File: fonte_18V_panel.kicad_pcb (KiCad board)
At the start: 2 copper layers, 210 x 176 mm, 210 parts, among them J1 MSTBA, J2 MSTBA, J3 RJ45_Shielded, J4 RJ45_Shielded, Q1 Si2308CDS, U1 LMR16030

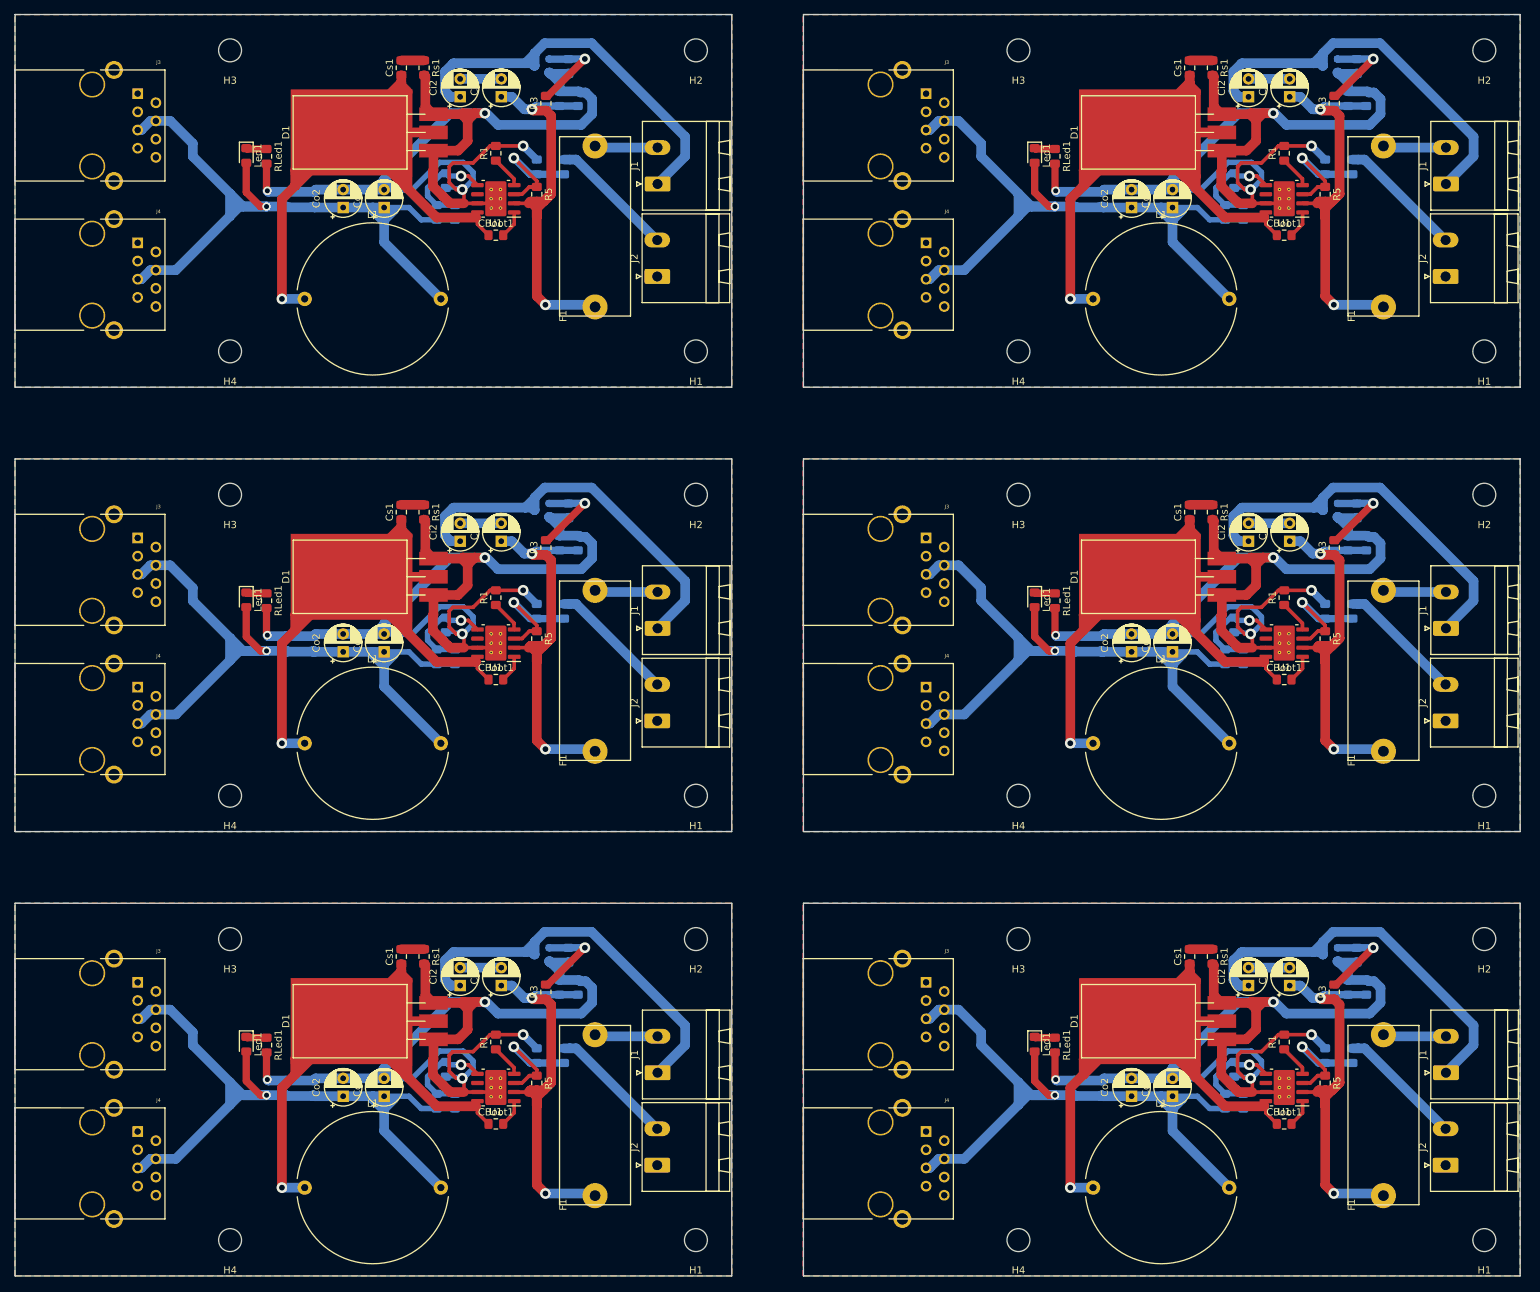
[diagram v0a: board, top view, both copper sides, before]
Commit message: Pads reforçados, algumas pequenas correções de regras
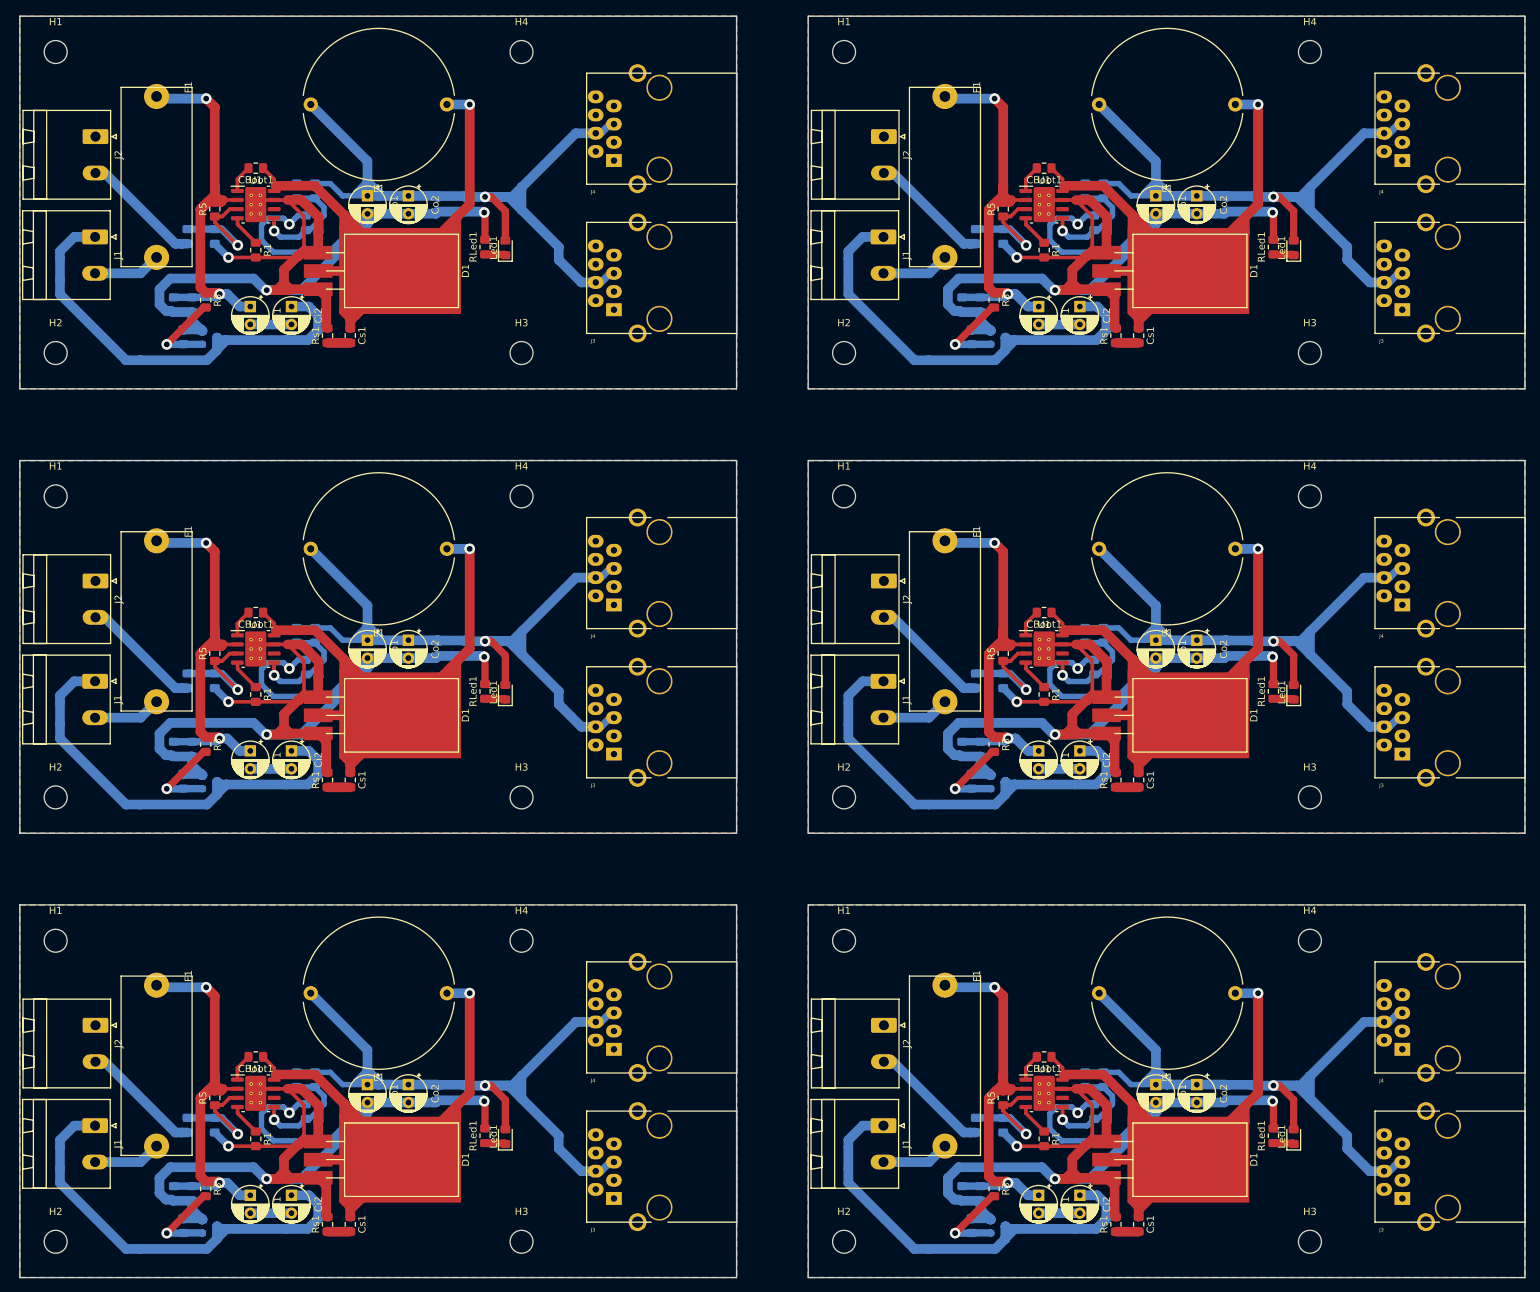
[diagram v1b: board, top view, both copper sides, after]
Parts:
- removed the CBoot1 at (221.8, 46.8)
- removed the CBoot1 at (221.8, 108.8)
- removed the CBoot1 at (221.8, 170.8)
- removed the CBoot1 at (111.8, 46.8)
- removed the CBoot1 at (111.8, 108.8)
- removed the Cff1 at (213.6, 43.6)
- removed the Cff1 at (213.6, 105.6)
- removed the Cff1 at (213.6, 167.6)
- removed the Cff1 at (103.6, 43.6)
- removed the Cff1 at (103.6, 105.6)
- removed the Ci1 at (222.6, 27.5)
- removed the Ci1 at (222.6, 89.5)
- removed the Ci1 at (222.6, 151.5)
- removed the Ci1 at (112.6, 27.5)
- removed the Ci1 at (112.6, 89.5)
- removed the Ci2 at (216.8, 27.5)
- removed the Ci2 at (216.8, 89.5)
- removed the Ci2 at (216.8, 151.5)
- removed the Ci2 at (106.8, 27.5)
- removed the Ci2 at (106.8, 89.5)
- removed the Cin2 at (230.7, 27.7)
- removed the Cin2 at (230.7, 89.7)
- removed the Cin2 at (230.7, 151.7)
- removed the Cin2 at (120.7, 27.7)
- removed the Cin2 at (120.7, 89.7)
- removed the Cin3 at (233.2, 27.7)
- removed the Cin3 at (233.2, 89.7)
- removed the Cin3 at (233.2, 151.7)
- removed the Cin3 at (123.2, 27.7)
- removed the Cin3 at (123.2, 89.7)
- removed the Co1 at (206.2, 42.9)
- removed the Co1 at (206.2, 104.9)
- removed the Co1 at (206.2, 166.9)
- removed the Co1 at (96.2, 42.9)
- removed the Co1 at (96.2, 104.9)
- removed the Co2 at (200.5, 42.9)
- removed the Co2 at (200.5, 104.9)
- removed the Co2 at (200.5, 166.9)
- removed the Co2 at (90.5, 42.9)
- removed the Co2 at (90.5, 104.9)
- removed the Co3 at (192.6, 41.7)
- removed the Co3 at (192.6, 103.7)
- removed the Co3 at (192.6, 165.7)
- removed the Co3 at (82.6, 41.7)
- removed the Co3 at (82.6, 103.7)
- removed the Co4 at (196.4, 41.7)
- removed the Co4 at (196.4, 103.7)
- removed the Co4 at (196.4, 165.7)
- removed the Co4 at (86.4, 41.7)
- removed the Co4 at (86.4, 103.7)
- removed the Cs1 at (208.6, 23.4)
- removed the Cs1 at (208.6, 85.4)
- removed the Cs1 at (208.6, 147.4)
- removed the Cs1 at (98.6, 23.4)
- removed the Cs1 at (98.6, 85.4)
- removed the D1 at (213.1, 35.0)
- removed the D1 at (213.1, 97.0)
- removed the D1 at (213.1, 159.0)
- removed the D1 at (103.1, 35.0)
- removed the D1 at (103.1, 97.0)
- removed the F1 at (230.7, 58.0)
- removed the F1 at (230.7, 120.0)
- removed the F1 at (230.7, 182.0)
- removed the F1 at (120.7, 58.0)
- removed the F1 at (120.7, 120.0)
- removed the H1 at (249.7, 63.0)
- removed the H1 at (249.7, 125.0)
- removed the H1 at (249.7, 187.0)
- removed the H1 at (139.7, 63.0)
- removed the H1 at (139.7, 125.0)
- removed the H2 at (249.7, 21.0)
- removed the H2 at (249.7, 83.0)
- removed the H2 at (249.7, 145.0)
- removed the H2 at (139.7, 21.0)
- removed the H2 at (139.7, 83.0)
- removed the H3 at (184.7, 21.0)
- removed the H3 at (184.7, 83.0)
- removed the H3 at (184.7, 145.0)
- removed the H3 at (74.7, 21.0)
- removed the H3 at (74.7, 83.0)
- removed the H4 at (184.7, 63.0)
- removed the H4 at (184.7, 125.0)
- removed the H4 at (184.7, 187.0)
- removed the H4 at (74.7, 63.0)
- removed the H4 at (74.7, 125.0)
- removed the J1 at (244.4, 39.6)
- removed the J1 at (244.4, 101.6)
- removed the J1 at (244.4, 163.6)
- removed the J1 at (134.4, 39.6)
- removed the J1 at (134.4, 101.6)
- removed the J1 at (134.4, 163.6)
- removed the J2 at (244.3, 52.5)
- removed the J2 at (244.3, 114.5)
- removed the J2 at (244.3, 176.5)
- removed the J2 at (134.3, 52.5)
- removed the J2 at (134.3, 114.5)
- removed the J2 at (134.3, 176.5)
- removed the J3 at (171.8, 27.0)
- removed the J3 at (171.8, 89.0)
- removed the J3 at (171.8, 151.0)
- removed the J3 at (61.8, 27.0)
- removed the J3 at (61.8, 89.0)
- removed the J4 at (171.8, 47.8)
- removed the J4 at (171.8, 109.8)
- removed the J4 at (171.8, 171.8)
- removed the J4 at (61.8, 47.8)
- removed the J4 at (61.8, 109.8)
- removed the L1 at (195.1, 55.6)
- removed the L1 at (195.1, 117.6)
- removed the L1 at (195.1, 179.6)
- removed the L1 at (85.1, 55.6)
- removed the L1 at (85.1, 117.6)
- removed the Led1 at (187.0, 35.6)
- removed the Led1 at (187.0, 97.6)
- removed the Led1 at (187.0, 159.6)
- removed the Led1 at (77.0, 35.6)
- removed the Led1 at (77.0, 97.6)
- removed the Q1 at (228.2, 23.1)
- removed the Q1 at (228.2, 85.1)
- removed the Q1 at (228.2, 147.1)
- removed the Q1 at (118.2, 23.1)
- removed the Q1 at (118.2, 85.1)
- removed the R1 at (221.8, 35.3)
- removed the R1 at (221.8, 97.3)
- removed the R1 at (221.8, 159.3)
- removed the R1 at (111.8, 35.3)
- removed the R1 at (111.8, 97.3)
- removed the R2 at (231.3, 37.2)
- removed the R2 at (231.3, 99.2)
- removed the R2 at (231.3, 161.2)
- removed the R2 at (121.3, 37.2)
- removed the R2 at (121.3, 99.2)
- removed the R3 at (228.8, 28.3)
- removed the R3 at (228.8, 90.3)
- removed the R3 at (228.8, 152.3)
- removed the R3 at (118.8, 28.3)
- removed the R3 at (118.8, 90.3)
- removed the R4 at (231.9, 23.2)
- removed the R4 at (231.9, 85.2)
- removed the R4 at (231.9, 147.2)
- removed the R4 at (121.9, 23.2)
- removed the R4 at (121.9, 85.2)
- removed the R5 at (227.5, 41.0)
- removed the R5 at (227.5, 103.0)
- removed the R5 at (227.5, 165.0)
- removed the R5 at (117.5, 41.0)
- removed the R5 at (117.5, 103.0)
- removed the R6 at (227.5, 37.2)
- removed the R6 at (227.5, 99.2)
- removed the R6 at (227.5, 161.2)
- removed the R6 at (117.5, 37.2)
- removed the R6 at (117.5, 99.2)
- removed the RLed1 at (189.8, 35.8)
- removed the RLed1 at (189.8, 97.8)
- removed the RLed1 at (189.8, 159.8)
- removed the RLed1 at (79.8, 35.8)
- removed the RLed1 at (79.8, 97.8)
- removed the Rfbb1 at (214.8, 39.1)
- removed the Rfbb1 at (214.8, 101.1)
- removed the Rfbb1 at (214.8, 163.1)
- removed the Rfbb1 at (104.8, 39.1)
- removed the Rfbb1 at (104.8, 101.1)
- removed the Rfbt2 at (216.1, 43.6)
- removed the Rfbt2 at (216.1, 105.6)
- removed the Rfbt2 at (216.1, 167.6)
- removed the Rfbt2 at (106.1, 43.6)
- removed the Rfbt2 at (106.1, 105.6)
- removed the Rs1 at (211.8, 23.4)
- removed the Rs1 at (211.8, 85.4)
- removed the Rs1 at (211.8, 147.4)
- removed the Rs1 at (101.8, 23.4)
- removed the Rs1 at (101.8, 85.4)
- removed the U1 at (221.8, 41.7)
- removed the U1 at (221.8, 103.7)
- removed the U1 at (221.8, 165.7)
- removed the U1 at (111.8, 41.7)
- removed the U1 at (111.8, 103.7)
- added CBoot1: 100nF, Capacitor_SMD:C_0805_2012Metric_Pad1.15x1.40mm_HandSolder, F.Cu at (188.3, 161.4)
- added CBoot1: 100nF, Capacitor_SMD:C_0805_2012Metric_Pad1.15x1.40mm_HandSolder, F.Cu at (78.3, 161.4)
- added CBoot1: 100nF, Capacitor_SMD:C_0805_2012Metric_Pad1.15x1.40mm_HandSolder, F.Cu at (188.3, 99.4)
- added CBoot1: 100nF, Capacitor_SMD:C_0805_2012Metric_Pad1.15x1.40mm_HandSolder, F.Cu at (78.3, 99.4)
- added CBoot1: 100nF, Capacitor_SMD:C_0805_2012Metric_Pad1.15x1.40mm_HandSolder, F.Cu at (188.3, 37.4)
- added Cff1: na, Capacitor_SMD:C_0805_2012Metric_Pad1.15x1.40mm_HandSolder, B.Cu at (196.6, 164.6)
- added Cff1: na, Capacitor_SMD:C_0805_2012Metric_Pad1.15x1.40mm_HandSolder, B.Cu at (86.6, 164.6)
- added Cff1: na, Capacitor_SMD:C_0805_2012Metric_Pad1.15x1.40mm_HandSolder, B.Cu at (196.6, 102.6)
- added Cff1: na, Capacitor_SMD:C_0805_2012Metric_Pad1.15x1.40mm_HandSolder, B.Cu at (86.6, 102.6)
- added Cff1: na, Capacitor_SMD:C_0805_2012Metric_Pad1.15x1.40mm_HandSolder, B.Cu at (196.6, 40.6)
- added Ci1: 10u, Capacitor_THT:CP_Radial_D5.0mm_P2.50mm, F.Cu at (187.6, 180.7)
- added Ci1: 10u, Capacitor_THT:CP_Radial_D5.0mm_P2.50mm, F.Cu at (77.6, 180.7)
- added Ci1: 10u, Capacitor_THT:CP_Radial_D5.0mm_P2.50mm, F.Cu at (187.6, 118.7)
- added Ci1: 10u, Capacitor_THT:CP_Radial_D5.0mm_P2.50mm, F.Cu at (77.6, 118.7)
- added Ci1: 10u, Capacitor_THT:CP_Radial_D5.0mm_P2.50mm, F.Cu at (187.6, 56.7)
- added Ci2: 10u, Capacitor_THT:CP_Radial_D5.0mm_P2.50mm, F.Cu at (193.3, 180.7)
- added Ci2: 10u, Capacitor_THT:CP_Radial_D5.0mm_P2.50mm, F.Cu at (83.3, 180.7)
- added Ci2: 10u, Capacitor_THT:CP_Radial_D5.0mm_P2.50mm, F.Cu at (193.3, 118.7)
- added Ci2: 10u, Capacitor_THT:CP_Radial_D5.0mm_P2.50mm, F.Cu at (83.3, 118.7)
- added Ci2: 10u, Capacitor_THT:CP_Radial_D5.0mm_P2.50mm, F.Cu at (193.3, 56.7)
- added Cin2: 100nF, Capacitor_SMD:C_0805_2012Metric_Pad1.15x1.40mm_HandSolder, B.Cu at (179.4, 180.5)
- added Cin2: 100nF, Capacitor_SMD:C_0805_2012Metric_Pad1.15x1.40mm_HandSolder, B.Cu at (69.4, 180.5)
- added Cin2: 100nF, Capacitor_SMD:C_0805_2012Metric_Pad1.15x1.40mm_HandSolder, B.Cu at (179.4, 118.5)
- added Cin2: 100nF, Capacitor_SMD:C_0805_2012Metric_Pad1.15x1.40mm_HandSolder, B.Cu at (69.4, 118.5)
- added Cin2: 100nF, Capacitor_SMD:C_0805_2012Metric_Pad1.15x1.40mm_HandSolder, B.Cu at (179.4, 56.5)
- added Cin3: 100nF, Capacitor_SMD:C_0805_2012Metric_Pad1.15x1.40mm_HandSolder, B.Cu at (176.9, 180.5)
- added Cin3: 100nF, Capacitor_SMD:C_0805_2012Metric_Pad1.15x1.40mm_HandSolder, B.Cu at (66.9, 180.5)
- added Cin3: 100nF, Capacitor_SMD:C_0805_2012Metric_Pad1.15x1.40mm_HandSolder, B.Cu at (176.9, 118.5)
- added Cin3: 100nF, Capacitor_SMD:C_0805_2012Metric_Pad1.15x1.40mm_HandSolder, B.Cu at (66.9, 118.5)
- added Cin3: 100nF, Capacitor_SMD:C_0805_2012Metric_Pad1.15x1.40mm_HandSolder, B.Cu at (176.9, 56.5)
- added Co1: 47u, Capacitor_THT:CP_Radial_D5.0mm_P2.50mm, F.Cu at (203.9, 165.3)
- added Co1: 47u, Capacitor_THT:CP_Radial_D5.0mm_P2.50mm, F.Cu at (93.9, 165.3)
- added Co1: 47u, Capacitor_THT:CP_Radial_D5.0mm_P2.50mm, F.Cu at (203.9, 103.3)
- added Co1: 47u, Capacitor_THT:CP_Radial_D5.0mm_P2.50mm, F.Cu at (93.9, 103.3)
- added Co1: 47u, Capacitor_THT:CP_Radial_D5.0mm_P2.50mm, F.Cu at (203.9, 41.3)
- added Co2: 47u, Capacitor_THT:CP_Radial_D5.0mm_P2.50mm, F.Cu at (209.6, 165.3)
- added Co2: 47u, Capacitor_THT:CP_Radial_D5.0mm_P2.50mm, F.Cu at (99.6, 165.3)
- added Co2: 47u, Capacitor_THT:CP_Radial_D5.0mm_P2.50mm, F.Cu at (209.6, 103.3)
- added Co2: 47u, Capacitor_THT:CP_Radial_D5.0mm_P2.50mm, F.Cu at (99.6, 103.3)
- added Co2: 47u, Capacitor_THT:CP_Radial_D5.0mm_P2.50mm, F.Cu at (209.6, 41.3)
- added Co3: o.1u, Capacitor_SMD:C_0805_2012Metric_Pad1.15x1.40mm_HandSolder, B.Cu at (217.6, 166.4)
- added Co3: o.1u, Capacitor_SMD:C_0805_2012Metric_Pad1.15x1.40mm_HandSolder, B.Cu at (107.6, 166.4)
- added Co3: o.1u, Capacitor_SMD:C_0805_2012Metric_Pad1.15x1.40mm_HandSolder, B.Cu at (217.6, 104.4)
- added Co3: o.1u, Capacitor_SMD:C_0805_2012Metric_Pad1.15x1.40mm_HandSolder, B.Cu at (107.6, 104.4)
- added Co3: o.1u, Capacitor_SMD:C_0805_2012Metric_Pad1.15x1.40mm_HandSolder, B.Cu at (217.6, 42.4)
- added Co4: 0.1u, Capacitor_SMD:C_0805_2012Metric_Pad1.15x1.40mm_HandSolder, B.Cu at (213.8, 166.4)
- added Co4: 0.1u, Capacitor_SMD:C_0805_2012Metric_Pad1.15x1.40mm_HandSolder, B.Cu at (103.8, 166.4)
- added Co4: 0.1u, Capacitor_SMD:C_0805_2012Metric_Pad1.15x1.40mm_HandSolder, B.Cu at (213.8, 104.4)
- added Co4: 0.1u, Capacitor_SMD:C_0805_2012Metric_Pad1.15x1.40mm_HandSolder, B.Cu at (103.8, 104.4)
- added Co4: 0.1u, Capacitor_SMD:C_0805_2012Metric_Pad1.15x1.40mm_HandSolder, B.Cu at (213.8, 42.4)
- added Cs1: 100n, Capacitor_SMD:C_0805_2012Metric_Pad1.15x1.40mm_HandSolder, F.Cu at (201.5, 184.8)
- added Cs1: 100n, Capacitor_SMD:C_0805_2012Metric_Pad1.15x1.40mm_HandSolder, F.Cu at (91.5, 184.8)
- added Cs1: 100n, Capacitor_SMD:C_0805_2012Metric_Pad1.15x1.40mm_HandSolder, F.Cu at (201.5, 122.8)
- added Cs1: 100n, Capacitor_SMD:C_0805_2012Metric_Pad1.15x1.40mm_HandSolder, F.Cu at (91.5, 122.8)
- added Cs1: 100n, Capacitor_SMD:C_0805_2012Metric_Pad1.15x1.40mm_HandSolder, F.Cu at (201.5, 60.8)
- added D1: MBR20200CTG, Package_TO_SOT_THT:TO-220-3_Horizontal_TabDown_SMD, F.Cu at (197.0, 173.2)
- added D1: MBR20200CTG, Package_TO_SOT_THT:TO-220-3_Horizontal_TabDown_SMD, F.Cu at (87.0, 173.2)
- added D1: MBR20200CTG, Package_TO_SOT_THT:TO-220-3_Horizontal_TabDown_SMD, F.Cu at (197.0, 111.2)
- added D1: MBR20200CTG, Package_TO_SOT_THT:TO-220-3_Horizontal_TabDown_SMD, F.Cu at (87.0, 111.2)
- added D1: MBR20200CTG, Package_TO_SOT_THT:TO-220-3_Horizontal_TabDown_SMD, F.Cu at (197.0, 49.2)
- added F1: 2A, KicadZeniteSolarLibrary18:Fuse_Holder_5x20, F.Cu at (179.4, 150.1)
- added F1: 2A, KicadZeniteSolarLibrary18:Fuse_Holder_5x20, F.Cu at (69.4, 150.1)
- added F1: 2A, KicadZeniteSolarLibrary18:Fuse_Holder_5x20, F.Cu at (179.4, 88.1)
- added F1: 2A, KicadZeniteSolarLibrary18:Fuse_Holder_5x20, F.Cu at (69.4, 88.1)
- added F1: 2A, KicadZeniteSolarLibrary18:Fuse_Holder_5x20, F.Cu at (179.4, 26.1)
- added H1: MountingHole, MountingHole:MountingHole_3.2mm_M3, F.Cu at (160.4, 145.2)
- added H1: MountingHole, MountingHole:MountingHole_3.2mm_M3, F.Cu at (50.4, 145.2)
- added H1: MountingHole, MountingHole:MountingHole_3.2mm_M3, F.Cu at (160.4, 83.2)
- added H1: MountingHole, MountingHole:MountingHole_3.2mm_M3, F.Cu at (50.4, 83.2)
- added H1: MountingHole, MountingHole:MountingHole_3.2mm_M3, F.Cu at (160.4, 21.2)
- added H2: MountingHole, MountingHole:MountingHole_3.2mm_M3, F.Cu at (160.4, 187.2)
- added H2: MountingHole, MountingHole:MountingHole_3.2mm_M3, F.Cu at (50.4, 187.2)
- added H2: MountingHole, MountingHole:MountingHole_3.2mm_M3, F.Cu at (160.4, 125.2)
- added H2: MountingHole, MountingHole:MountingHole_3.2mm_M3, F.Cu at (50.4, 125.2)
- added H2: MountingHole, MountingHole:MountingHole_3.2mm_M3, F.Cu at (160.4, 63.2)
- added H3: MountingHole, MountingHole:MountingHole_3.2mm_M3, F.Cu at (225.4, 187.2)
- added H3: MountingHole, MountingHole:MountingHole_3.2mm_M3, F.Cu at (115.4, 187.2)
- added H3: MountingHole, MountingHole:MountingHole_3.2mm_M3, F.Cu at (225.4, 125.2)
- added H3: MountingHole, MountingHole:MountingHole_3.2mm_M3, F.Cu at (115.4, 125.2)
- added H3: MountingHole, MountingHole:MountingHole_3.2mm_M3, F.Cu at (225.4, 63.2)
- added H4: MountingHole, MountingHole:MountingHole_3.2mm_M3, F.Cu at (225.4, 145.2)
- added H4: MountingHole, MountingHole:MountingHole_3.2mm_M3, F.Cu at (115.4, 145.2)
- added H4: MountingHole, MountingHole:MountingHole_3.2mm_M3, F.Cu at (225.4, 83.2)
- added H4: MountingHole, MountingHole:MountingHole_3.2mm_M3, F.Cu at (115.4, 83.2)
- added H4: MountingHole, MountingHole:MountingHole_3.2mm_M3, F.Cu at (225.4, 21.2)
- added J1: MSTBA, Connector_Phoenix_MSTB:PhoenixContact_MSTBA_2,5_2-G-5,08_1x02_P5.08mm_Horizontal, F.Cu at (165.9, 171.0)
- added J1: MSTBA, Connector_Phoenix_MSTB:PhoenixContact_MSTBA_2,5_2-G-5,08_1x02_P5.08mm_Horizontal, F.Cu at (55.9, 171.0)
- added J1: MSTBA, Connector_Phoenix_MSTB:PhoenixContact_MSTBA_2,5_2-G-5,08_1x02_P5.08mm_Horizontal, F.Cu at (165.9, 109.0)
- added J1: MSTBA, Connector_Phoenix_MSTB:PhoenixContact_MSTBA_2,5_2-G-5,08_1x02_P5.08mm_Horizontal, F.Cu at (55.9, 109.0)
- added J1: MSTBA, Connector_Phoenix_MSTB:PhoenixContact_MSTBA_2,5_2-G-5,08_1x02_P5.08mm_Horizontal, F.Cu at (165.9, 47.0)
- added J1: MSTBA, Connector_Phoenix_MSTB:PhoenixContact_MSTBA_2,5_2-G-5,08_1x02_P5.08mm_Horizontal, F.Cu at (55.9, 47.0)
- added J2: MSTBA, Connector_Phoenix_MSTB:PhoenixContact_MSTBA_2,5_2-G-5,08_1x02_P5.08mm_Horizontal, F.Cu at (166.0, 157.0)
- added J2: MSTBA, Connector_Phoenix_MSTB:PhoenixContact_MSTBA_2,5_2-G-5,08_1x02_P5.08mm_Horizontal, F.Cu at (56.0, 157.0)
- added J2: MSTBA, Connector_Phoenix_MSTB:PhoenixContact_MSTBA_2,5_2-G-5,08_1x02_P5.08mm_Horizontal, F.Cu at (166.0, 95.0)
- added J2: MSTBA, Connector_Phoenix_MSTB:PhoenixContact_MSTBA_2,5_2-G-5,08_1x02_P5.08mm_Horizontal, F.Cu at (56.0, 95.0)
- added J2: MSTBA, Connector_Phoenix_MSTB:PhoenixContact_MSTBA_2,5_2-G-5,08_1x02_P5.08mm_Horizontal, F.Cu at (166.0, 33.0)
- added J2: MSTBA, Connector_Phoenix_MSTB:PhoenixContact_MSTBA_2,5_2-G-5,08_1x02_P5.08mm_Horizontal, F.Cu at (56.0, 33.0)
- added J3: RJ45_Shielded, MFP19RJ45:RJ45_YH59_01, F.Cu at (238.3, 181.2)
- added J3: RJ45_Shielded, MFP19RJ45:RJ45_YH59_01, F.Cu at (128.3, 181.2)
- added J3: RJ45_Shielded, MFP19RJ45:RJ45_YH59_01, F.Cu at (238.3, 119.2)
- added J3: RJ45_Shielded, MFP19RJ45:RJ45_YH59_01, F.Cu at (128.3, 119.2)
- added J3: RJ45_Shielded, MFP19RJ45:RJ45_YH59_01, F.Cu at (238.3, 57.2)
- added J4: RJ45_Shielded, MFP19RJ45:RJ45_YH59_01, F.Cu at (238.3, 160.3)
- added J4: RJ45_Shielded, MFP19RJ45:RJ45_YH59_01, F.Cu at (128.3, 160.3)
- added J4: RJ45_Shielded, MFP19RJ45:RJ45_YH59_01, F.Cu at (238.3, 98.3)
- added J4: RJ45_Shielded, MFP19RJ45:RJ45_YH59_01, F.Cu at (128.3, 98.3)
- added J4: RJ45_Shielded, MFP19RJ45:RJ45_YH59_01, F.Cu at (238.3, 36.4)
- added L1: 100uH, Inductor_THT:L_Radial_D21.0mm_P19.00mm, F.Cu at (215.0, 152.5)
- added L1: 100uH, Inductor_THT:L_Radial_D21.0mm_P19.00mm, F.Cu at (105.0, 152.5)
- added L1: 100uH, Inductor_THT:L_Radial_D21.0mm_P19.00mm, F.Cu at (215.0, 90.5)
- added L1: 100uH, Inductor_THT:L_Radial_D21.0mm_P19.00mm, F.Cu at (105.0, 90.5)
- added L1: 100uH, Inductor_THT:L_Radial_D21.0mm_P19.00mm, F.Cu at (215.0, 28.5)
- added Led1: LED, LED_SMD:LED_0805_2012Metric_Pad1.15x1.40mm_HandSolder, F.Cu at (223.1, 172.5)
- added Led1: LED, LED_SMD:LED_0805_2012Metric_Pad1.15x1.40mm_HandSolder, F.Cu at (113.1, 172.5)
- added Led1: LED, LED_SMD:LED_0805_2012Metric_Pad1.15x1.40mm_HandSolder, F.Cu at (223.1, 110.5)
- added Led1: LED, LED_SMD:LED_0805_2012Metric_Pad1.15x1.40mm_HandSolder, F.Cu at (113.1, 110.5)
- added Led1: LED, LED_SMD:LED_0805_2012Metric_Pad1.15x1.40mm_HandSolder, F.Cu at (223.1, 48.5)
- added Q1: Si2308CDS, Package_TO_SOT_SMD:SOT-23, B.Cu at (181.9, 185.1)
- added Q1: Si2308CDS, Package_TO_SOT_SMD:SOT-23, B.Cu at (71.9, 185.1)
- added Q1: Si2308CDS, Package_TO_SOT_SMD:SOT-23, B.Cu at (181.9, 123.0)
- added Q1: Si2308CDS, Package_TO_SOT_SMD:SOT-23, B.Cu at (71.9, 123.0)
- added Q1: Si2308CDS, Package_TO_SOT_SMD:SOT-23, B.Cu at (181.9, 61.0)
- added R1: 47k, Resistor_SMD:R_0805_2012Metric_Pad1.15x1.40mm_HandSolder, F.Cu at (188.3, 172.8)
- added R1: 47k, Resistor_SMD:R_0805_2012Metric_Pad1.15x1.40mm_HandSolder, F.Cu at (78.3, 172.8)
- added R1: 47k, Resistor_SMD:R_0805_2012Metric_Pad1.15x1.40mm_HandSolder, F.Cu at (188.3, 110.8)
- added R1: 47k, Resistor_SMD:R_0805_2012Metric_Pad1.15x1.40mm_HandSolder, F.Cu at (78.3, 110.8)
- added R1: 47k, Resistor_SMD:R_0805_2012Metric_Pad1.15x1.40mm_HandSolder, F.Cu at (188.3, 48.8)
- added R2: 100, Resistor_SMD:R_0805_2012Metric_Pad1.15x1.40mm_HandSolder, B.Cu at (178.8, 170.9)
- added R2: 100, Resistor_SMD:R_0805_2012Metric_Pad1.15x1.40mm_HandSolder, B.Cu at (68.8, 170.9)
- added R2: 100, Resistor_SMD:R_0805_2012Metric_Pad1.15x1.40mm_HandSolder, B.Cu at (178.8, 108.9)
- added R2: 100, Resistor_SMD:R_0805_2012Metric_Pad1.15x1.40mm_HandSolder, B.Cu at (68.8, 108.9)
- added R2: 100, Resistor_SMD:R_0805_2012Metric_Pad1.15x1.40mm_HandSolder, B.Cu at (178.8, 46.9)
- added R3: 220K, Resistor_SMD:R_0805_2012Metric_Pad1.15x1.40mm_HandSolder, F.Cu at (181.3, 179.8)
- added R3: 220K, Resistor_SMD:R_0805_2012Metric_Pad1.15x1.40mm_HandSolder, F.Cu at (71.3, 179.8)
- added R3: 220K, Resistor_SMD:R_0805_2012Metric_Pad1.15x1.40mm_HandSolder, F.Cu at (181.3, 117.8)
- added R3: 220K, Resistor_SMD:R_0805_2012Metric_Pad1.15x1.40mm_HandSolder, F.Cu at (71.3, 117.8)
- added R3: 220K, Resistor_SMD:R_0805_2012Metric_Pad1.15x1.40mm_HandSolder, F.Cu at (181.3, 55.8)
- added R4: 100K, Resistor_SMD:R_0805_2012Metric_Pad1.15x1.40mm_HandSolder, B.Cu at (178.2, 184.9)
- added R4: 100K, Resistor_SMD:R_0805_2012Metric_Pad1.15x1.40mm_HandSolder, B.Cu at (68.2, 184.9)
- added R4: 100K, Resistor_SMD:R_0805_2012Metric_Pad1.15x1.40mm_HandSolder, B.Cu at (178.2, 123.0)
- added R4: 100K, Resistor_SMD:R_0805_2012Metric_Pad1.15x1.40mm_HandSolder, B.Cu at (68.2, 123.0)
- added R4: 100K, Resistor_SMD:R_0805_2012Metric_Pad1.15x1.40mm_HandSolder, B.Cu at (178.2, 61.0)
- added R5: 10K, Resistor_SMD:R_0805_2012Metric_Pad1.15x1.40mm_HandSolder, F.Cu at (182.6, 167.1)
- added R5: 10K, Resistor_SMD:R_0805_2012Metric_Pad1.15x1.40mm_HandSolder, F.Cu at (72.6, 167.1)
- added R5: 10K, Resistor_SMD:R_0805_2012Metric_Pad1.15x1.40mm_HandSolder, F.Cu at (182.6, 105.1)
- added R5: 10K, Resistor_SMD:R_0805_2012Metric_Pad1.15x1.40mm_HandSolder, F.Cu at (72.6, 105.1)
- added R5: 10K, Resistor_SMD:R_0805_2012Metric_Pad1.15x1.40mm_HandSolder, F.Cu at (182.6, 43.1)
- added R6: NA, Resistor_SMD:R_0805_2012Metric_Pad1.15x1.40mm_HandSolder, B.Cu at (182.6, 170.9)
- added R6: NA, Resistor_SMD:R_0805_2012Metric_Pad1.15x1.40mm_HandSolder, B.Cu at (72.6, 170.9)
- added R6: NA, Resistor_SMD:R_0805_2012Metric_Pad1.15x1.40mm_HandSolder, B.Cu at (182.6, 108.9)
- added R6: NA, Resistor_SMD:R_0805_2012Metric_Pad1.15x1.40mm_HandSolder, B.Cu at (72.6, 108.9)
- added R6: NA, Resistor_SMD:R_0805_2012Metric_Pad1.15x1.40mm_HandSolder, B.Cu at (182.6, 46.9)
- added RLed1: 1k5, Resistor_SMD:R_0805_2012Metric_Pad1.15x1.40mm_HandSolder, F.Cu at (220.3, 172.4)
- added RLed1: 1k5, Resistor_SMD:R_0805_2012Metric_Pad1.15x1.40mm_HandSolder, F.Cu at (110.3, 172.4)
- added RLed1: 1k5, Resistor_SMD:R_0805_2012Metric_Pad1.15x1.40mm_HandSolder, F.Cu at (220.3, 110.4)
- added RLed1: 1k5, Resistor_SMD:R_0805_2012Metric_Pad1.15x1.40mm_HandSolder, F.Cu at (110.3, 110.4)
- added RLed1: 1k5, Resistor_SMD:R_0805_2012Metric_Pad1.15x1.40mm_HandSolder, F.Cu at (220.3, 48.4)
- added Rfbb1: 8k2, Resistor_SMD:R_0805_2012Metric_Pad1.15x1.40mm_HandSolder, B.Cu at (195.3, 169.0)
- added Rfbb1: 8k2, Resistor_SMD:R_0805_2012Metric_Pad1.15x1.40mm_HandSolder, B.Cu at (85.3, 169.0)
- added Rfbb1: 8k2, Resistor_SMD:R_0805_2012Metric_Pad1.15x1.40mm_HandSolder, B.Cu at (195.3, 107.0)
- added Rfbb1: 8k2, Resistor_SMD:R_0805_2012Metric_Pad1.15x1.40mm_HandSolder, B.Cu at (85.3, 107.0)
- added Rfbb1: 8k2, Resistor_SMD:R_0805_2012Metric_Pad1.15x1.40mm_HandSolder, B.Cu at (195.3, 45.0)
- added Rfbt2: 230k, Resistor_SMD:R_0805_2012Metric_Pad1.15x1.40mm_HandSolder, B.Cu at (194.0, 164.6)
- added Rfbt2: 230k, Resistor_SMD:R_0805_2012Metric_Pad1.15x1.40mm_HandSolder, B.Cu at (84.0, 164.6)
- added Rfbt2: 230k, Resistor_SMD:R_0805_2012Metric_Pad1.15x1.40mm_HandSolder, B.Cu at (194.0, 102.6)
- added Rfbt2: 230k, Resistor_SMD:R_0805_2012Metric_Pad1.15x1.40mm_HandSolder, B.Cu at (84.0, 102.6)
- added Rfbt2: 230k, Resistor_SMD:R_0805_2012Metric_Pad1.15x1.40mm_HandSolder, B.Cu at (194.0, 40.6)
- added Rs1: 2k2, Resistor_SMD:R_0805_2012Metric_Pad1.15x1.40mm_HandSolder, F.Cu at (198.3, 184.8)
- added Rs1: 2k2, Resistor_SMD:R_0805_2012Metric_Pad1.15x1.40mm_HandSolder, F.Cu at (88.3, 184.8)
- added Rs1: 2k2, Resistor_SMD:R_0805_2012Metric_Pad1.15x1.40mm_HandSolder, F.Cu at (198.3, 122.8)
- added Rs1: 2k2, Resistor_SMD:R_0805_2012Metric_Pad1.15x1.40mm_HandSolder, F.Cu at (88.3, 122.8)
- added Rs1: 2k2, Resistor_SMD:R_0805_2012Metric_Pad1.15x1.40mm_HandSolder, F.Cu at (198.3, 60.8)
- added U1: LMR16030, Package_SO:Texas_R-PDSO-G8_EP2.95x4.9mm_Mask2.4x3.1mm_ThermalVias, F.Cu at (188.3, 166.5)
- added U1: LMR16030, Package_SO:Texas_R-PDSO-G8_EP2.95x4.9mm_Mask2.4x3.1mm_ThermalVias, F.Cu at (78.3, 166.5)
- added U1: LMR16030, Package_SO:Texas_R-PDSO-G8_EP2.95x4.9mm_Mask2.4x3.1mm_ThermalVias, F.Cu at (188.3, 104.5)
- added U1: LMR16030, Package_SO:Texas_R-PDSO-G8_EP2.95x4.9mm_Mask2.4x3.1mm_ThermalVias, F.Cu at (78.3, 104.5)
- added U1: LMR16030, Package_SO:Texas_R-PDSO-G8_EP2.95x4.9mm_Mask2.4x3.1mm_ThermalVias, F.Cu at (188.3, 42.5)
- moved H1 188.3 mm to (50.4, 21.2), turned to 0 degrees
- moved H4 170.7 mm to (115.4, 21.2), turned to 0 degrees
- moved F1 164.1 mm to (69.4, 26.1), turned to 270 degrees
- moved L1 152.4 mm to (105.0, 28.5), turned to 180 degrees
- moved J4 150.9 mm to (128.3, 36.4), turned to 90 degrees
- moved CBoot1 137.5 mm to (78.3, 37.4), turned to 180 degrees
- moved R5 129.9 mm to (72.6, 43.1), turned to 90 degrees
- moved Rfbt2 128.9 mm to (84.0, 40.6), turned to 270 degrees
- moved Cff1 128.1 mm to (86.6, 40.6), turned to 270 degrees
- moved U1 127.7 mm to (78.3, 42.5), turned to 0 degrees
- moved Co2 126.0 mm to (99.6, 41.3), turned to 270 degrees
- moved Co3 125.8 mm to (107.6, 42.4), turned to 270 degrees
- moved R2 125.8 mm to (68.8, 46.9), turned to 270 degrees
- moved Co1 125.6 mm to (93.9, 41.3), turned to 270 degrees
- moved Co4 124.5 mm to (103.8, 42.4), turned to 270 degrees
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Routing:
- net GND: track 958.6 -> 1004.0 mm
- net Net-(Ci2-Pad1): track 343.0 -> 376.6 mm
- net /Feedback: track 87.2 -> 94.9 mm
- net Net-(J2-Pad2): track 105.9 -> 101.6 mm
- net Net-(F1-Pad2): track 52.9 -> 57.0 mm
